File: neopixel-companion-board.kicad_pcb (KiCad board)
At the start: 2 copper layers, 59.9 x 52.4 mm, 22 parts, among them J1 Conn_01x03, J2 Conn_01x03, J3 Conn_01x03, J4 Conn_01x03, J5 VIN, J6 Conn_01x04, U1 74LVC1G17, U2 74LVC1G17, U3 74LVC1G17, U4 74LVC1G17

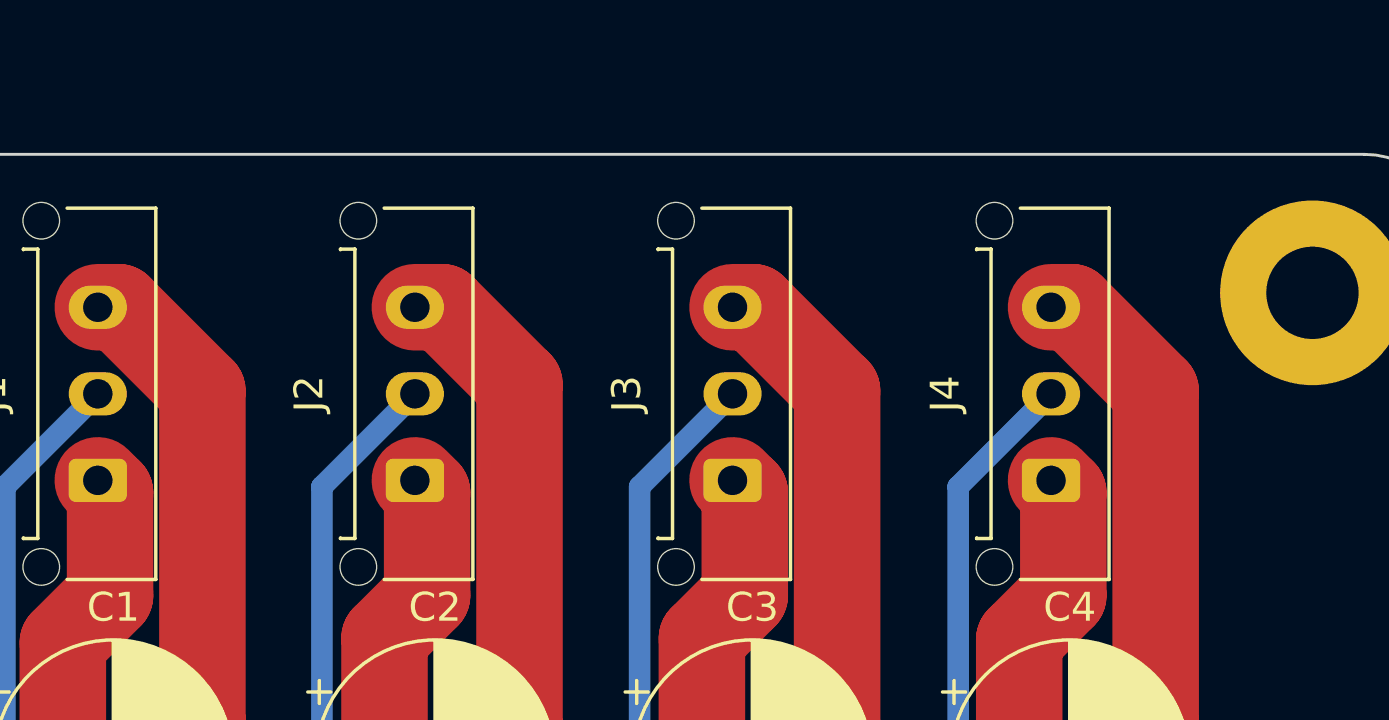
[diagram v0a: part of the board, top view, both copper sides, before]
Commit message: Added molex connector models and text
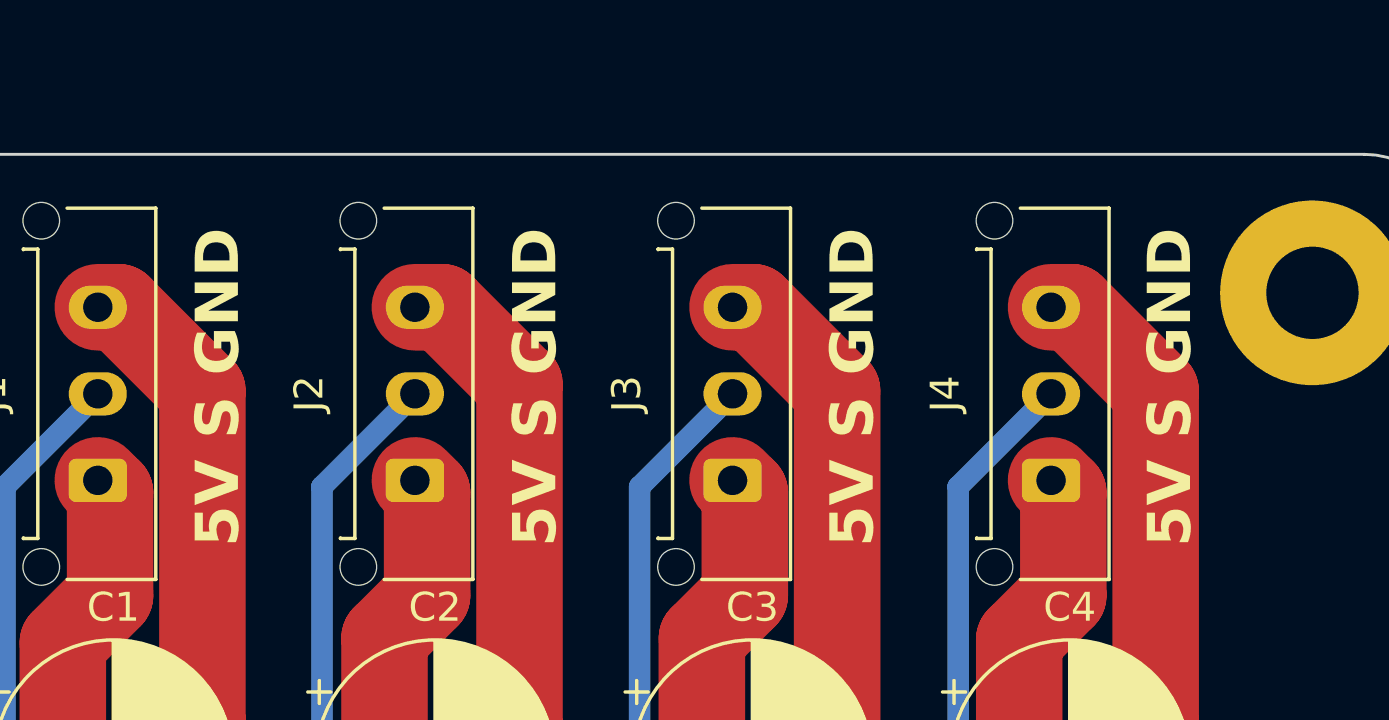
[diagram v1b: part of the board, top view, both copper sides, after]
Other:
- board text added: "5V S GND"
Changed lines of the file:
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@@
     (pad "3" thru_hole oval (at 6 0 90) (size 1.5 2.02) (drill 1.02) (layers "*.Cu" "*.Mask")
       (net 2 "GND") (pinfunction "Pin_3") (pintype "passive"))
-    (model "${KICAD6_3DMODEL_DIR}/Connector_Molex.3dshapes/Molex_Micro-Fit_3.0_43650-0315_1x03_P3.00mm_Vertical.wrl"
+    (model "${KICAD6_3DMODEL_DIR}/Connector_Molex.3dshapes/Molex_Micro-Fit_3.0_43650-0315_1x03_P3.00mm_Vertical.wrl" hide
       (offset (xyz 0 0 0))
       (scale (xyz 1 1 1))
       (rotate (xyz 0 0 0))
+    )
+    (model "d:/NextCloud/3D-Druck/V-core custom/neopixel-companion-board/436500315.stp"
+      (offset (xyz 3 2 10))
+      (scale (xyz 1 1 1))
+      (rotate (xyz 90 0 180))
     )
   )
@@
     (pad "3" thru_hole oval (at 6 0 90) (size 1.5 2.02) (drill 1.02) (layers "*.Cu" "*.Mask")
       (net 2 "GND") (pinfunction "Pin_3") (pintype "passive"))
-    (model "${KICAD6_3DMODEL_DIR}/Connector_Molex.3dshapes/Molex_Micro-Fit_3.0_43650-0315_1x03_P3.00mm_Vertical.wrl"
+    (model "${KICAD6_3DMODEL_DIR}/Connector_Molex.3dshapes/Molex_Micro-Fit_3.0_43650-0315_1x03_P3.00mm_Vertical.wrl" hide
       (offset (xyz 0 0 0))
       (scale (xyz 1 1 1))
       (rotate (xyz 0 0 0))
+    )
+    (model "d:/NextCloud/3D-Druck/V-core custom/neopixel-companion-board/436500315.stp"
+      (offset (xyz 3 2 10))
+      (scale (xyz 1 1 1))
+      (rotate (xyz 90 0 180))
     )
   )
@@
     (pad "3" thru_hole oval (at 6 0 90) (size 1.5 2.02) (drill 1.02) (layers "*.Cu" "*.Mask")
       (net 2 "GND") (pinfunction "Pin_3") (pintype "passive"))
-    (model "${KICAD6_3DMODEL_DIR}/Connector_Molex.3dshapes/Molex_Micro-Fit_3.0_43650-0315_1x03_P3.00mm_Vertical.wrl"
-      (offset (xyz 0 0 0))
+    (model "${KICAD6_3DMODEL_DIR}/Connector_Molex.3dshapes/Molex_Micro-Fit_3.0_43650-0315_1x03_P3.00mm_Vertical.wrl" hide
+      (offset (xyz 3 2 10))
       (scale (xyz 1 1 1))
       (rotate (xyz 0 0 0))
+    )
+    (model "d:/NextCloud/3D-Druck/V-core custom/neopixel-companion-board/436500315.stp"
+      (offset (xyz 3 2 10))
+      (scale (xyz 1 1 1))
+      (rotate (xyz 90 0 180))
     )
   )
@@
     (pad "3" thru_hole oval (at 6 0 90) (size 1.5 2.02) (drill 1.02) (layers "*.Cu" "*.Mask")
       (net 2 "GND") (pinfunction "Pin_3") (pintype "passive"))
-    (model "${KICAD6_3DMODEL_DIR}/Connector_Molex.3dshapes/Molex_Micro-Fit_3.0_43650-0315_1x03_P3.00mm_Vertical.wrl"
+    (model "${KICAD6_3DMODEL_DIR}/Connector_Molex.3dshapes/Molex_Micro-Fit_3.0_43650-0315_1x03_P3.00mm_Vertical.wrl" hide
       (offset (xyz 0 0 0))
       (scale (xyz 1 1 1))
       (rotate (xyz 0 0 0))
+    )
+    (model "d:/NextCloud/3D-Druck/V-core custom/neopixel-companion-board/436500315.stp"
+      (offset (xyz 3 2 10))
+      (scale (xyz 1 1 1))
+      (rotate (xyz 90 0 180))
     )
   )
@@
     (stroke (width 0.1) (type solid)) (layer "Edge.Cuts"))
   (gr_text "1" (at 80.95 74) (layer "F.SilkS")
+    (effects (font (size 1.5 1.5) (thickness 0.3) bold) (justify left bottom))
+  )
+  (gr_text "5V S GND" (at 85.5 43.8 90) (layer "F.SilkS")
     (effects (font (size 1.5 1.5) (thickness 0.3) bold) (justify left bottom))
   )
@@
     (effects (font (size 1.5 1.5) (thickness 0.3) bold) (justify left bottom))
   )
+  (gr_text "5V S GND" (at 96.5 43.8 90) (layer "F.SilkS")
+    (effects (font (size 1.5 1.5) (thickness 0.3) bold) (justify left bottom))
+  )
   (gr_text "3" (at 85.95 74) (layer "F.SilkS")
     (effects (font (size 1.5 1.5) (thickness 0.3) bold) (justify left bottom))
   )
+  (gr_text "5V S GND" (at 107.5 43.8 90) (layer "F.SilkS")
+    (effects (font (size 1.5 1.5) (thickness 0.3) bold) (justify left bottom))
+  )
+  (gr_text "5V S GND" (at 118.5 43.8 90) (layer "F.SilkS")
+    (effects (font (size 1.5 1.5) (thickness 0.3) bold) (justify left bottom))
+  )

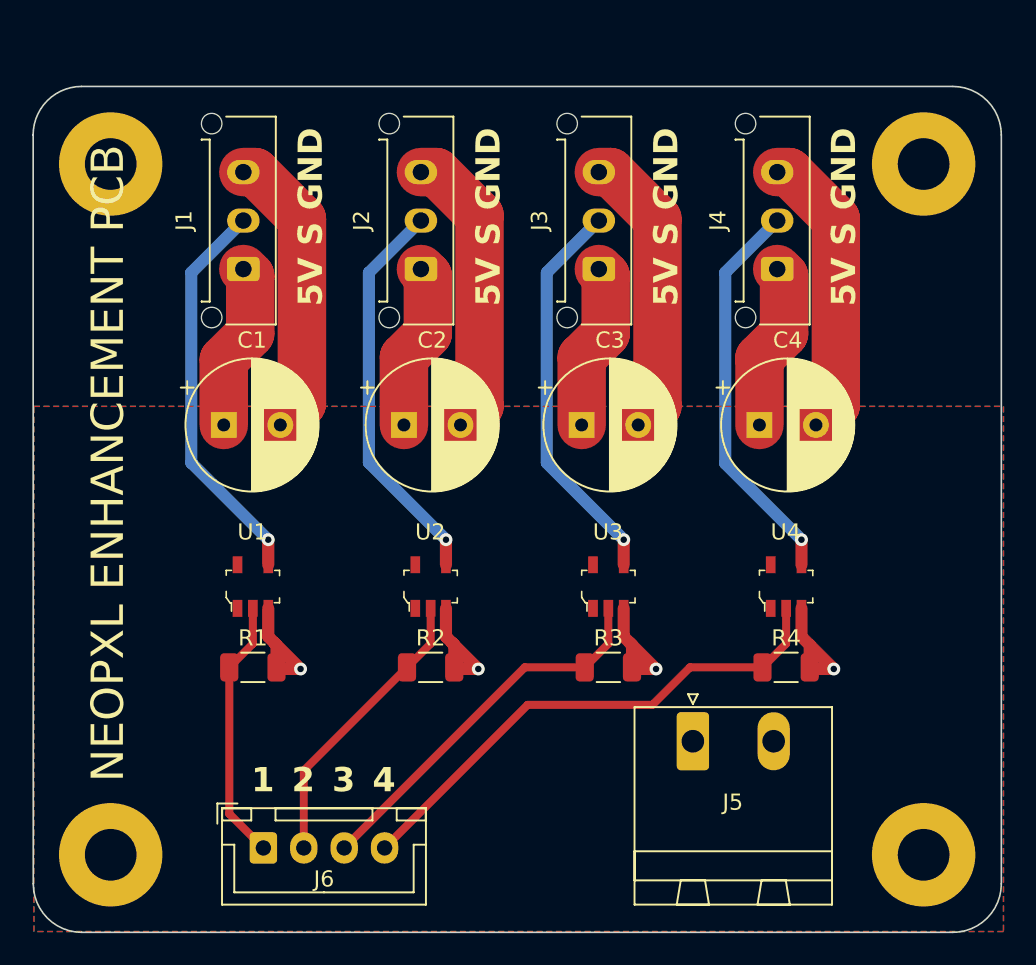
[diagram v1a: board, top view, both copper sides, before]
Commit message: Changed connector and added library files
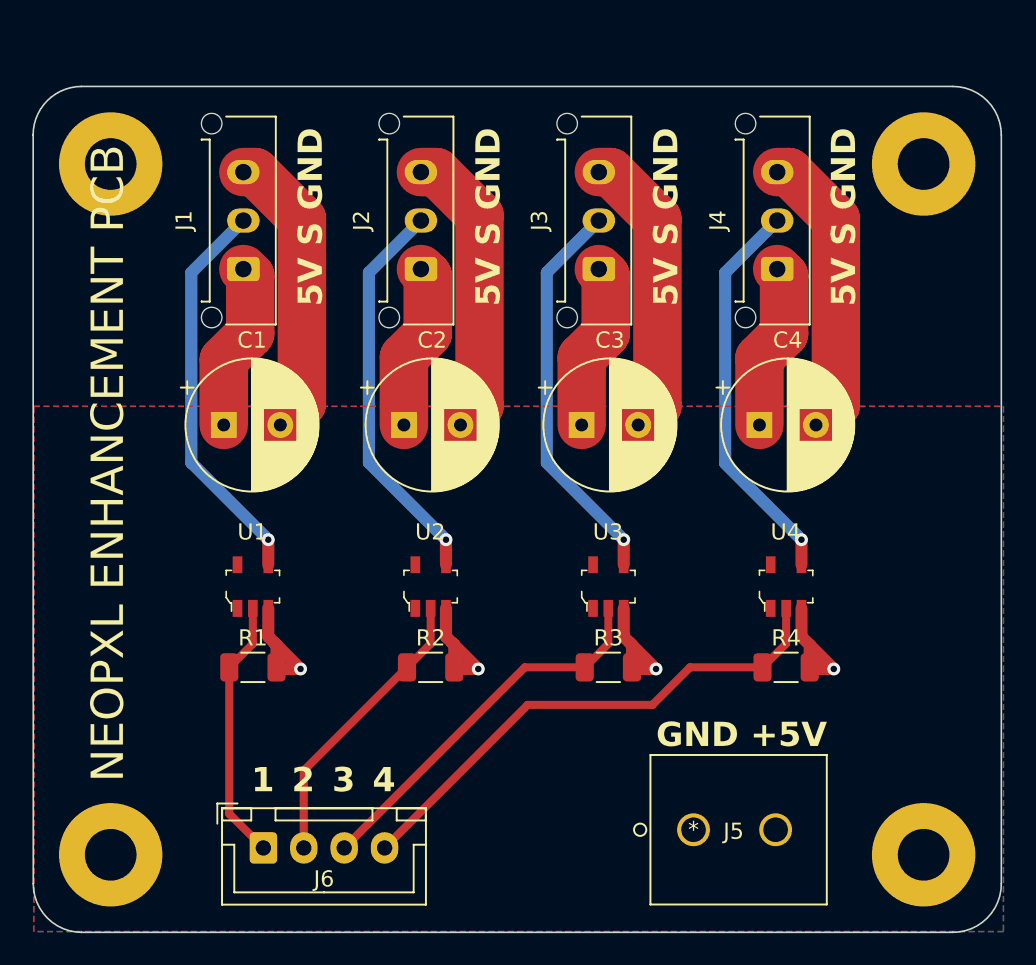
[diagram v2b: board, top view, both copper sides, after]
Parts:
- J5: footprint Connector_Phoenix_MSTB:PhoenixContact_MSTBA_2,5_2-G_1x02_P5.00mm_Horizontal -> Neopixel-Companion:796949-2
- U1, U2, U3, U4: footprint KlipperExpander:SOT-753 -> Neopixel-Companion:SOT-753
- moved J5 5.48 mm to (108.3, 76.2)
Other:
- board text added: "GND +5V"

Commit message: Replaced single schmitt triggers with a 4 bit level shifter
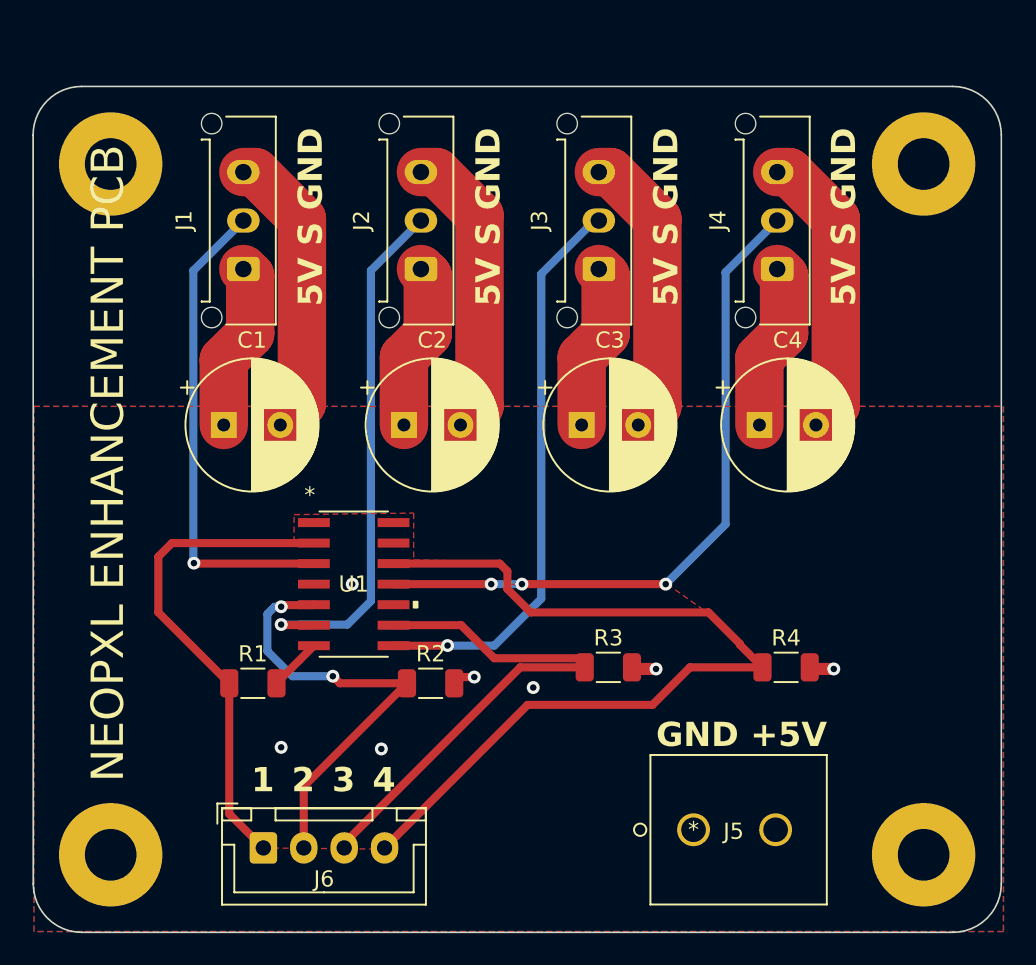
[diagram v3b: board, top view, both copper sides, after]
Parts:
- removed U2, U3, U4: 74LVC1G17, Neopixel-Companion:SOT-753
- J1: value Conn_01x03 -> PXL_1_Output
- J2: value Conn_01x03 -> PXL_2_Output
- J3: value Conn_01x03 -> PXL_3_Output
- J4: value Conn_01x03 -> PXL_4_Output
- J6: value Conn_01x04 -> PXL_Input
- U1: value 74LVC1G17 -> SN74AHCT125D; footprint Neopixel-Companion:SOT-753 -> Neopixel-Companion:SN74AHCT125D
- moved U1 6.24 mm to (87.3, 61.0)
- moved R1 0.99 mm to (81.0, 67.1)
- moved R2 0.99 mm to (92.0, 67.1)
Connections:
- J1 pad 2: Net-(J1-Pin_2) -> Neopixel_1_5V
- J2 pad 2: Net-(J2-Pin_2) -> Neopixel_2_5V
- J3 pad 2: Net-(J3-Pin_2) -> Neopixel_3_5V
- J4 pad 2: Net-(J4-Pin_2) -> Neopixel_4_5V
- U1 pad 1: (no net) -> GND
- U1 pad 3: GND -> Neopixel_1_5V
- U1 pad 4: Net-(J1-Pin_2) -> GND
- U1 pad 5: +5V -> Neopixel_2
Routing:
- net Neopixel_4_5V: track 0.00 -> 42.2 mm, vias 0 -> 3
- net Neopixel_3_5V: track 0.00 -> 35.4 mm, vias 0 -> 1
- net Neopixel_2_5V: track 0.00 -> 33.0 mm, vias 0 -> 1
- net Neopixel_1_5V: track 0.00 -> 29.7 mm, vias 0 -> 1
- net Net-(J2-Pin_2): track 24.6 -> 0.00 mm, vias 1 -> 0
- net Net-(J3-Pin_2): track 24.6 -> 0.00 mm, vias 1 -> 0
- net Net-(J1-Pin_2): track 24.6 -> 0.00 mm, vias 1 -> 0
- net Net-(J4-Pin_2): track 24.6 -> 0.00 mm, vias 1 -> 0
- net GND: track 103.1 -> 80.2 mm, vias 4 -> 7
- net Neopixel_4: track 32.3 -> 54.2 mm
- net Neopixel_1: track 16.3 -> 30.7 mm
- net Neopixel_2: track 18.1 -> 27.7 mm, vias 0 -> 2
- net Neopixel_3: track 23.8 -> 32.9 mm
- added copper zone on F.Cu, net GND

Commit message: Added LCSC parts and gerbers
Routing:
- net GND: track 80.2 -> 74.2 mm
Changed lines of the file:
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@@
     (descr "Resistor SMD 1206 (3216 Metric), square (rectangular) end terminal, IPC_7351 nominal, (Body size source: IPC-SM-782 page 72, https://www.pcb-3d.com/wordpress/wp-content/uploads/ipc-sm-782a_amendment_1_and_2.pdf), generated with kicad-footprint-generator")
     (tags "resistor")
+    (property "LCSC" "C104821")
     (property "Sheetfile" "neopixel-companion-board.kicad_sch")
     (property "Sheetname" "")
@@
     (descr "Resistor SMD 1206 (3216 Metric), square (rectangular) end terminal, IPC_7351 nominal, (Body size source: IPC-SM-782 page 72, https://www.pcb-3d.com/wordpress/wp-content/uploads/ipc-sm-782a_amendment_1_and_2.pdf), generated with kicad-footprint-generator")
     (tags "resistor")
+    (property "LCSC" "C104821")
     (property "Sheetfile" "neopixel-companion-board.kicad_sch")
     (property "Sheetname" "")
@@
     (descr "Resistor SMD 1206 (3216 Metric), square (rectangular) end terminal, IPC_7351 nominal, (Body size source: IPC-SM-782 page 72, https://www.pcb-3d.com/wordpress/wp-content/uploads/ipc-sm-782a_amendment_1_and_2.pdf), generated with kicad-footprint-generator")
     (tags "resistor")
+    (property "LCSC" "C104821")
     (property "Sheetfile" "neopixel-companion-board.kicad_sch")
     (property "Sheetname" "")
@@
     (descr "Resistor SMD 1206 (3216 Metric), square (rectangular) end terminal, IPC_7351 nominal, (Body size source: IPC-SM-782 page 72, https://www.pcb-3d.com/wordpress/wp-content/uploads/ipc-sm-782a_amendment_1_and_2.pdf), generated with kicad-footprint-generator")
     (tags "resistor")
+    (property "LCSC" "C104821")
     (property "Sheetfile" "neopixel-companion-board.kicad_sch")
     (property "Sheetname" "")
@@
   (footprint "Neopixel-Companion:SN74AHCT125D" (layer "F.Cu")
     (at 87.29 61)
+    (property "LCSC" "C155176")
     (property "Sheetfile" "neopixel-companion-board.kicad_sch")
     (property "Sheetname" "")
@@
   (segment (start 117.125 49.922349) (end 117.125 38.400177) (width 3) (layer "F.Cu") (net 2))
   (segment (start 84.085 49.812349) (end 82.747349 51.15) (width 3) (layer "F.Cu") (net 2))
-  (segment (start 106 66.25) (end 104.6125 66.25) (width 0.75) (layer "F.Cu") (net 2))
   (segment (start 95.075 49.972349) (end 93.897349 51.15) (width 3) (layer "F.Cu") (net 2))
   (segment (start 117.125 49.922349) (end 115.897349 51.15) (width 3) (layer "F.Cu") (net 2))
@@
   (segment (start 84.085 49.812349) (end 84.085 38.400177) (width 3) (layer "F.Cu") (net 2))
   (segment (start 106.085 49.962349) (end 106.085 38.400177) (width 3) (layer "F.Cu") (net 2))
-  (segment (start 93.8987 66.75) (end 93.5125 67.1362) (width 0.5) (layer "F.Cu") (net 2))
   (segment (start 117 66.25) (end 115.6125 66.25) (width 0.75) (layer "F.Cu") (net 2))
   (segment (start 82.5125 67.1362) (end 82.5125 67.1237) (width 0.5) (layer "F.Cu") (net 2))
   (segment (start 95.075 38.175) (end 92.4 35.5) (width 3) (layer "F.Cu") (net 2))
-  (segment (start 94.75 66.75) (end 93.8987 66.75) (width 0.5) (layer "F.Cu") (net 2))
   (segment (start 114.224823 35.5) (end 113.5 35.5) (width 3) (layer "F.Cu") (net 2))
   (segment (start 95.075 49.972349) (end 95.075 38.175) (width 3) (layer "F.Cu") (net 2))
@@
   (segment (start 103.184823 35.5) (end 102.46 35.5) (width 3) (layer "F.Cu") (net 2))
   (segment (start 104.897349 51.15) (end 106.085 49.962349) (width 3) (layer "F.Cu") (net 2))
-  (segment (start 82.5125 67.1237) (end 84.8262 64.81) (width 0.5) (layer "F.Cu") (net 2))
   (segment (start 92.4 35.5) (end 91.45 35.5) (width 3) (layer "F.Cu") (net 2))
   (via (at 117 66.25) (size 0.8) (drill 0.4) (layers "F.Cu" "B.Cu") (free) (net 2))
   (via (at 89 71.2) (size 0.8) (drill 0.4) (layers "F.Cu" "B.Cu") (free) (net 2))
   (via (at 82.8 71.1) (size 0.8) (drill 0.4) (layers "F.Cu" "B.Cu") (free) (net 2))
-  (via (at 106 66.25) (size 0.8) (drill 0.4) (layers "F.Cu" "B.Cu") (free) (net 2))
+  (via (at 107.1 64.5) (size 0.8) (drill 0.4) (layers "F.Cu" "B.Cu") (free) (net 2))
+  (via (at 79 62.4) (size 0.8) (drill 0.4) (layers "F.Cu" "B.Cu") (free) (net 2))
   (via (at 98.4 67.4) (size 0.8) (drill 0.4) (layers "F.Cu" "B.Cu") (free) (net 2))
   (via (at 87.2 61) (size 0.8) (drill 0.4) (layers "F.Cu" "B.Cu") (free) (net 2))
-  (via (at 94.75 66.75) (size 0.8) (drill 0.4) (layers "F.Cu" "B.Cu") (free) (net 2))
   (segment (start 84.8262 58.46) (end 76.04 58.46) (width 0.5) (layer "F.Cu") (net 3))
   (segment (start 81.7 77.325) (end 79.5875 75.2125) (width 0.5) (layer "F.Cu") (net 3))
